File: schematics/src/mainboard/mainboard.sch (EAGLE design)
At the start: 73 parts, among them IC1 566, IC2 TL074P, IC4 4013N, IC5 TL072P, IC6 TL072P, Q1 2N3904, Q2 2N3906, Q3 2N3904, Q4 2N3904, Q5 BF245

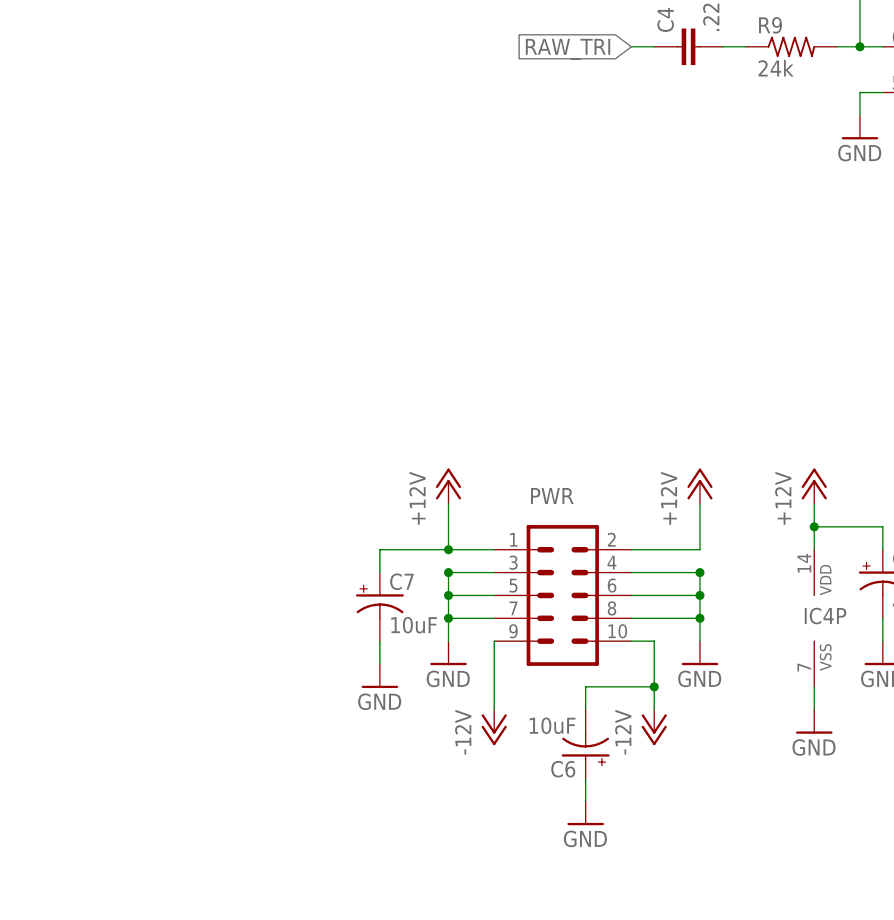
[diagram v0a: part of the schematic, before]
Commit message: Updated Schematics, Fixed Power Socket orientation
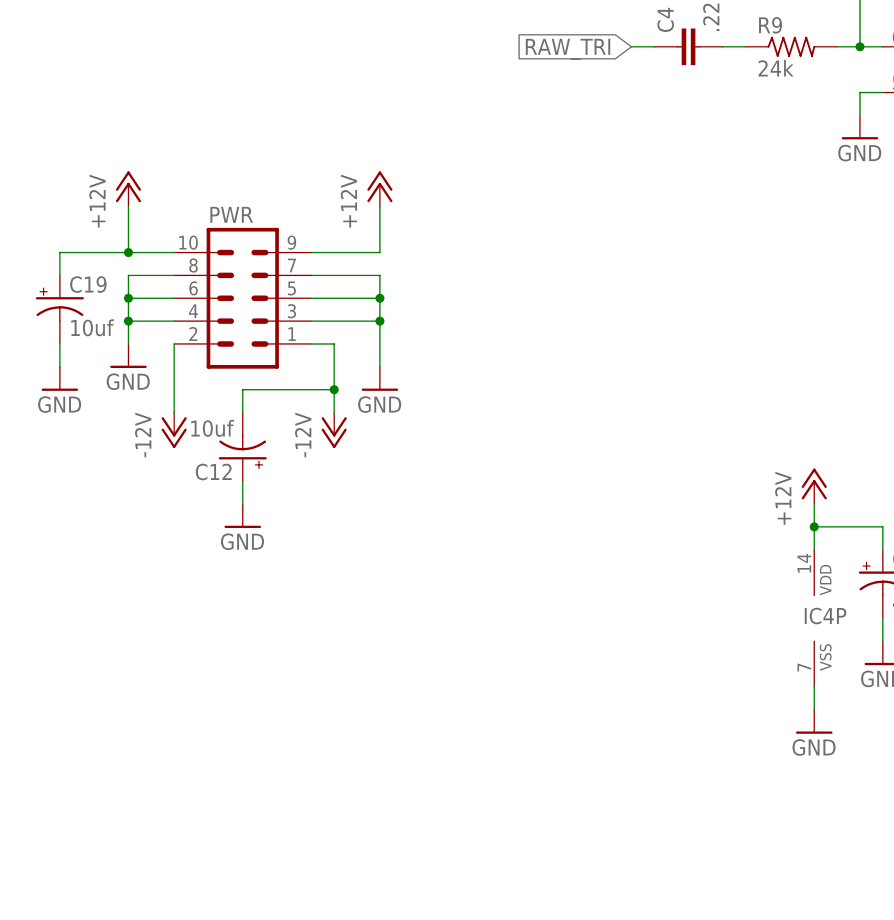
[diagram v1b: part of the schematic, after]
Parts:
- removed C6, C7: 10uF, resistor:CPOL-USE2.5-5
- added C12, C19: 10uf, resistor:CPOL-USE2.5-5
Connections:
- net +12V: now also C19.+, PWR.10, PWR.9; no longer C7.+, PWR.1, PWR.2
- net -12V: now also C12.-, PWR.1, PWR.2; no longer C6.-, PWR.10, PWR.9
- net GND: now also C12.+, C19.-; no longer C6.+, C7.-
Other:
- moved on the sheet: PWR

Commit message: Fixed minor issues, added documentation and updated some faceplates
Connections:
- net -12V: now also C2.-; no longer C2.+
- net GND: now also C2.+; no longer C2.-
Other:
- moved on the sheet: C2
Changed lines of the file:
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@@
 <attribute name="VALUE" x="61.595" y="166.37" size="1.778" layer="96"/>
 </instance>
-<instance part="C2" gate="G$1" x="63.5" y="185.42" smashed="yes" rot="R90">
-<attribute name="NAME" x="62.865" y="186.436" size="1.778" layer="95" rot="R90"/>
-<attribute name="VALUE" x="67.691" y="186.436" size="1.778" layer="96" rot="R90"/>
+<instance part="C2" gate="G$1" x="66.04" y="185.42" smashed="yes" rot="R270">
+<attribute name="NAME" x="60.325" y="186.436" size="1.778" layer="95" rot="R90"/>
+<attribute name="VALUE" x="62.611" y="186.436" size="1.778" layer="96" rot="R90"/>
 </instance>
 <instance part="P-1" gate="1" x="50.8" y="180.34" smashed="yes">
@@
 <net name="GND" class="0">
 <segment>
-<wire x1="68.58" y1="185.42" x2="76.2" y2="185.42" width="0.1524" layer="91"/>
 <pinref part="IC1" gate="G$1" pin="8"/>
 <wire x1="73.66" y1="177.8" x2="76.2" y2="177.8" width="0.1524" layer="91"/>
@@
 <wire x1="76.2" y1="185.42" x2="91.44" y2="185.42" width="0.1524" layer="91"/>
 <wire x1="91.44" y1="185.42" x2="91.44" y2="182.88" width="0.1524" layer="91"/>
+<pinref part="C2" gate="G$1" pin="+"/>
+<wire x1="68.58" y1="185.42" x2="76.2" y2="185.42" width="0.1524" layer="91"/>
 <junction x="76.2" y="185.42"/>
-<pinref part="C2" gate="G$1" pin="-"/>
 </segment>
 <segment>
@@
 <wire x1="58.42" y1="177.8" x2="55.88" y2="177.8" width="0.1524" layer="91"/>
 <wire x1="55.88" y1="177.8" x2="55.88" y2="185.42" width="0.1524" layer="91"/>
+<wire x1="50.8" y1="185.42" x2="55.88" y2="185.42" width="0.1524" layer="91"/>
+<pinref part="C2" gate="G$1" pin="-"/>
 <wire x1="55.88" y1="185.42" x2="60.96" y2="185.42" width="0.1524" layer="91"/>
-<wire x1="50.8" y1="185.42" x2="55.88" y2="185.42" width="0.1524" layer="91"/>
 <junction x="55.88" y="185.42"/>
-<pinref part="C2" gate="G$1" pin="+"/>
-</segment>
-<segment>
+</segment>
+<segment>

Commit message: Fixed some bugs and updated documentation
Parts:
- R32, R37: value 1.5k -> 3k
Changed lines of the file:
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@@
 <part name="R30" library="resistor" deviceset="R-US_" device="0204/7" value="2.2m"/>
 <part name="R31" library="resistor" deviceset="R-US_" device="0204/7" value="3k"/>
-<part name="R32" library="resistor" deviceset="R-US_" device="0204/7" value="1.5k"/>
+<part name="R32" library="resistor" deviceset="R-US_" device="0204/7" value="3k"/>
 <part name="R33" library="resistor" deviceset="R-US_" device="0204/7" value="10k"/>
 <part name="R34" library="resistor" deviceset="R-US_" device="0204/7" value="10k"/>
@@
 <part name="R35" library="resistor" deviceset="R-US_" device="0204/7" value="2.2m"/>
 <part name="R36" library="resistor" deviceset="R-US_" device="0204/7" value="3k"/>
-<part name="R37" library="resistor" deviceset="R-US_" device="0204/7" value="1.5k"/>
+<part name="R37" library="resistor" deviceset="R-US_" device="0204/7" value="3k"/>
 <part name="R38" library="resistor" deviceset="R-US_" device="0204/7" value="10k"/>
 <part name="R39" library="resistor" deviceset="R-US_" device="0204/7" value="10k"/>
